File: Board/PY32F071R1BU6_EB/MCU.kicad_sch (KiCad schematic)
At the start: 2 parts, among them J2 Conn_02x05_Odd_Even, U1 PY32F071R1BU

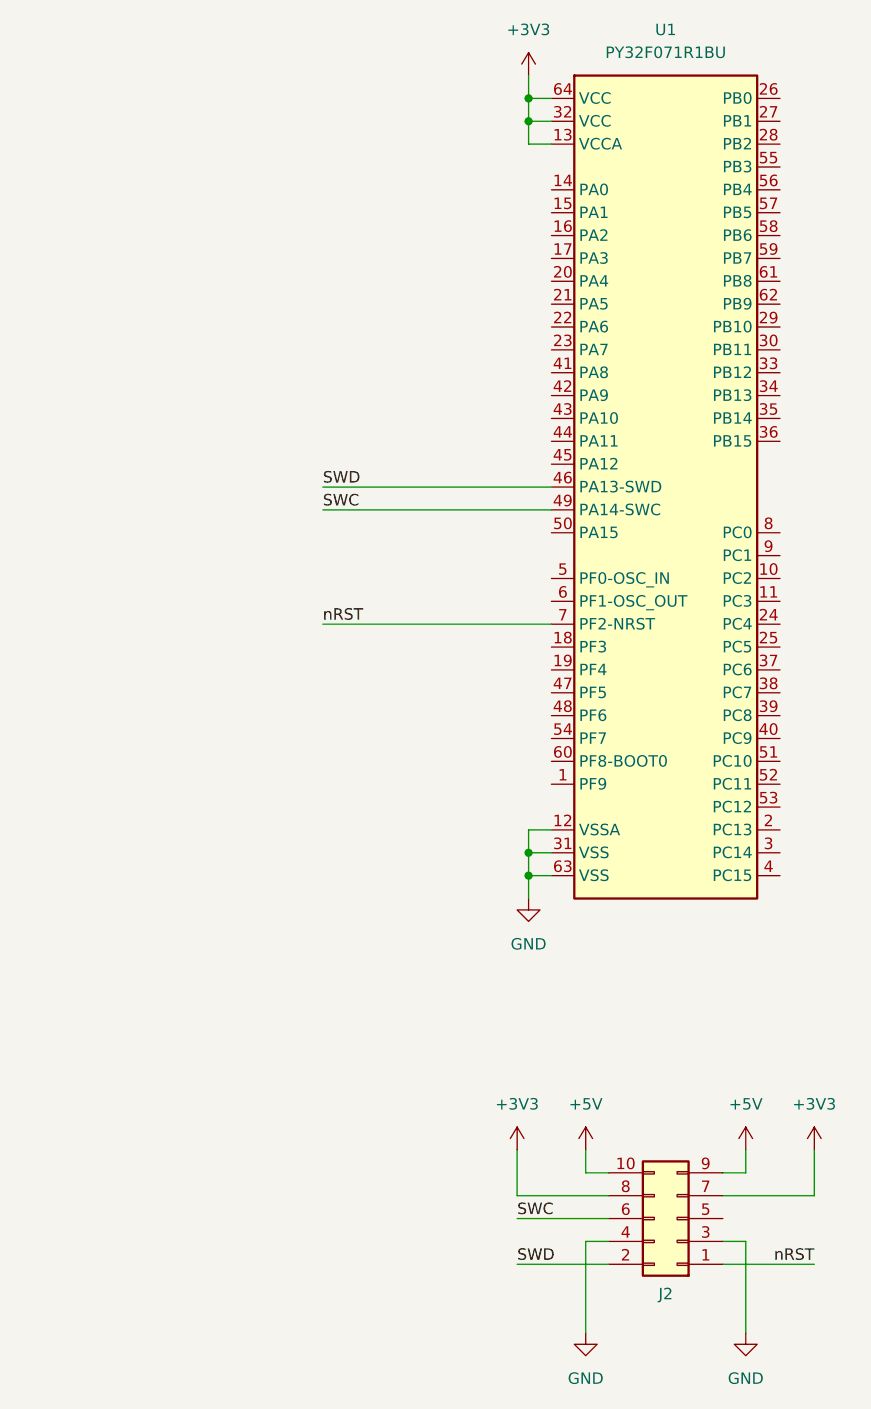
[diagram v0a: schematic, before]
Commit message: Power circuit prepared
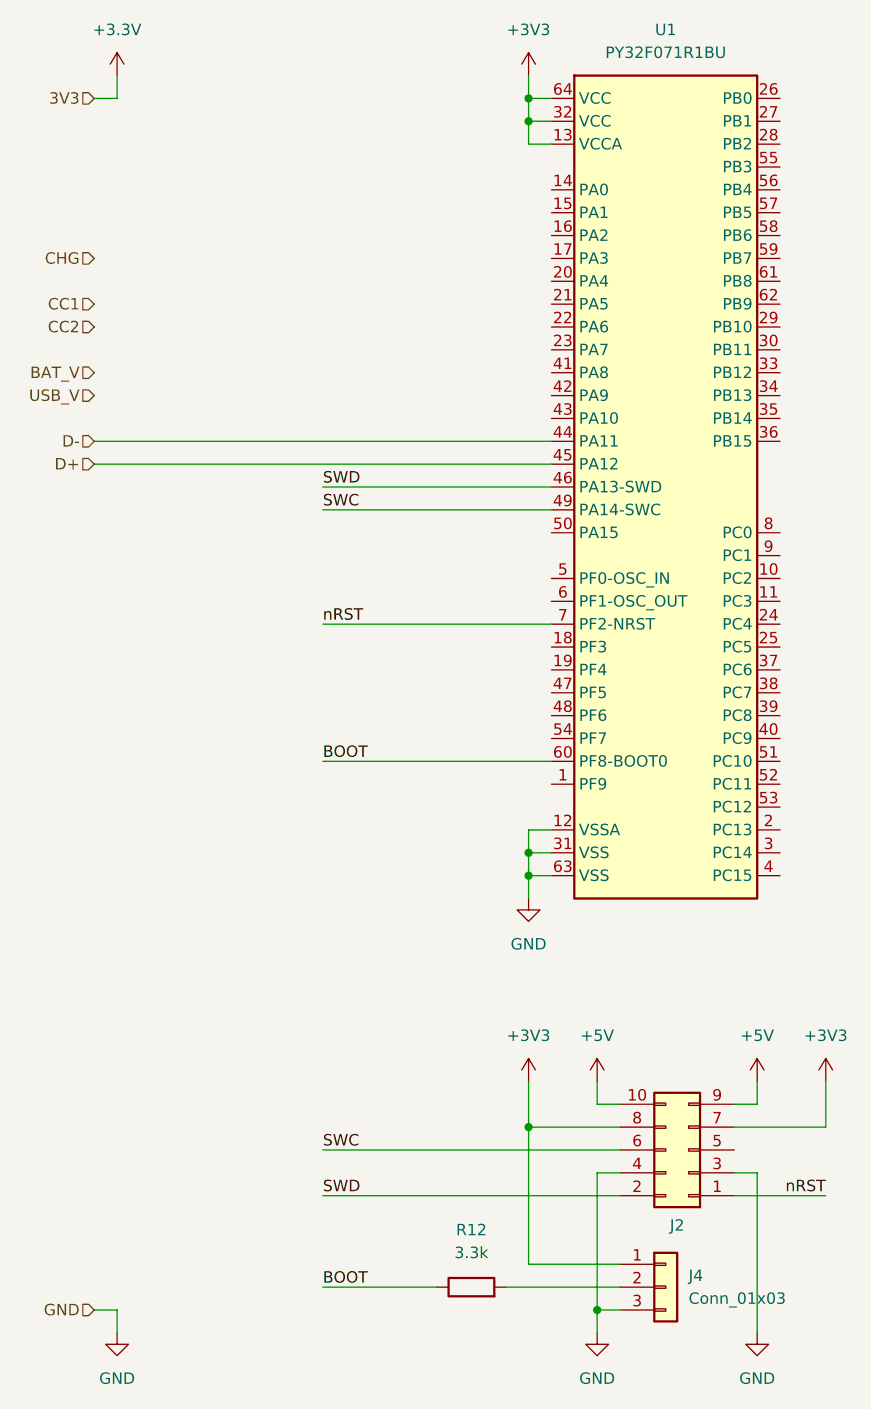
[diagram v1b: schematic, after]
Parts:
- added J4: Conn_01x03, Connector_PinHeader_2.54mm:PinHeader_1x03_P2.54mm_Vertical, symbol Connector_Generic:Conn_01x03
- added R12: 3.3k, Resistor_SMD:R_0603_1608Metric_Pad0.98x0.95mm_HandSolder, symbol Device:R
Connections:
- net +3V3: now also J4.1 (Pin_1)
- net GND: now also J4.3 (Pin_3)
- net D-: now reaches U1.44 (PA11)
- net D+: now reaches U1.45 (PA12)
- net BOOT: now reaches U1.60 (PF8-BOOT0)
- net BOOT: now also R12.1
- new net: J4.2 (Pin_2), R12.2
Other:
- moved on the sheet: J2

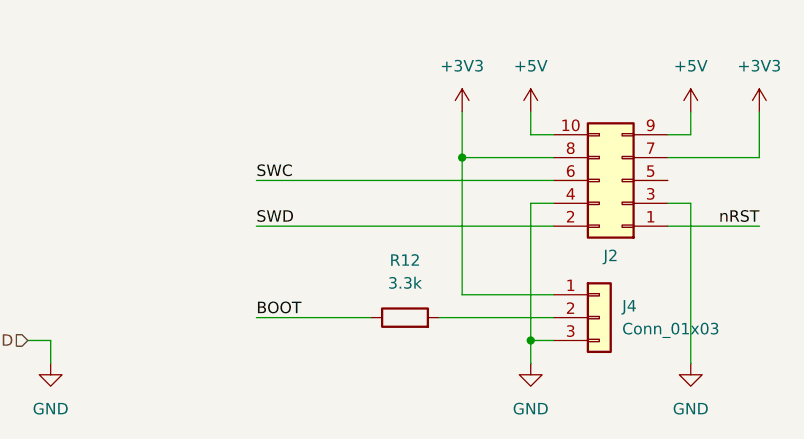
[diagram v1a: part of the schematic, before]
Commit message: Display added to schematic
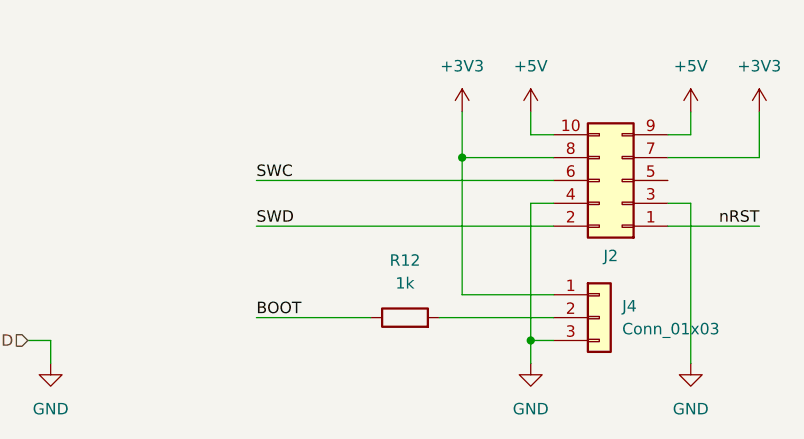
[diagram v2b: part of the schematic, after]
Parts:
- R12: value 3.3k -> 1k
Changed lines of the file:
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@@
 			)
 		)
-		(property "Value" "3.3k"
+		(property "Value" "1k"
 			(at 118.11 168.91 90)
 			(effects

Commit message: Schematic updated
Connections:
- net BAT_V: now also U1.15 (PA1)
- net CC1: now also U1.17 (PA3), U1.18 (PF3)
- net CC2: now also U1.19 (PF4), U1.20 (PA4)
- net CHG: now also U1.50 (PA15)
- net USB_V: now also U1.16 (PA2)
- net BTN1: now reaches U1.10 (PC2)
- net BTN2: now reaches U1.11 (PC3)
- net SCL: now reaches U1.21 (PA5)
- net BLK: now reaches U1.22 (PA6)
- net D0: now reaches U1.23 (PA7)
- net RESX: now reaches U1.41 (PA8)
- net DCX: now reaches U1.42 (PA9)
- net CSX: now reaches U1.43 (PA10)
- net LED0: now reaches U1.47 (PF5)
- net LED1: now reaches U1.48 (PF6)
- net OSC_IN: now reaches U1.5 (PF0-OSC_IN)
- net LED2: now reaches U1.54 (PF7)
- net OSC_OUT: now reaches U1.6 (PF1-OSC_OUT)
- net FREQ: now reaches U1.8 (PC0)
- net BTN0: now reaches U1.9 (PC1)
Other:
- note added: "ADC_IN1"
- note added: "ADC_IN2"
- note added: "ADC_IN3"
- note added: "ADC_IN4"
- note added: "COMP1_INP0"
- note added: "SPI1_MOSI"
- note added: "SPI1_SCK"
- note added: "TIM16_CH1"
- note added: "USBD_D+"
- note added: "USBD_D-"

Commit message: Component placement started
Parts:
- added C12, C13, C14: 1uF, Capacitor_SMD:C_0603_1608Metric_Pad1.08x0.95mm_HandSolder, symbol Device:C
- added J8, J9: Conn_01x16, Connector_PinHeader_2.54mm:PinHeader_1x16_P2.54mm_Vertical, symbol Connector_Generic:Conn_01x16
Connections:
- net +3V3: now also C12.1, C13.1, C14.1
- net GND: now also U1.65 (EP), C12.2, C13.2, C14.2
- net PB0: now reaches U1.26 (PB0)
- net PB1: now reaches U1.27 (PB1)
- net PB2: now reaches U1.28 (PB2)
- net PB10: now reaches U1.29 (PB10)
- net PB11: now reaches U1.30 (PB11)
- net PB12: now reaches U1.33 (PB12)
- net PB13: now reaches U1.34 (PB13)
- net PB14: now reaches U1.35 (PB14)
- net PB15: now reaches U1.36 (PB15)
- net PB3: now reaches U1.55 (PB3)
- net PB3: now also J9.7 (Pin_7)
- net PB4: now reaches U1.56 (PB4)
- net PB4: now also J9.6 (Pin_6)
- net PB5: now reaches U1.57 (PB5)
- net PB5: now also J9.5 (Pin_5)
- net PB6: now reaches U1.58 (PB6)
- net PB6: now also J9.4 (Pin_4)
- net PB7: now reaches U1.59 (PB7)
- net PB7: now also J9.3 (Pin_3)
- net PB8: now reaches U1.61 (PB8)
- net PB8: now also J9.2 (Pin_2)
- net PB9: now reaches U1.62 (PB9)
- net PB9: now also J9.1 (Pin_1)
